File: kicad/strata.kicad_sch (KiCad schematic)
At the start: 107 parts, among them J1 Eurorack Mono Jack, J10 Conn_01x04_Male, J11 Conn_01x04_Male, J12 Conn_01x04_Female, J13 Conn_01x08_Male, J14 Eurorack Mono Jack, J15 Conn_01x08_Female, J16 Eurorack Mono Jack, J17 Eurorack Mono Jack, J18 Eurorack Mono Jack, J19 Eurorack Mono Jack, J2 Eurorack Mono Jack, J20 Eurorack Mono Jack, J24 Eurorack Mono Jack, J25 Eurorack Mono Jack, J26 Eurorack Mono Jack, J27 Eurorack Mono Jack, J28 Eurorack Mono Jack, J29 Eurorack Mono Jack, J3 Eurorack Mono Jack, J30 Eurorack Mono Jack, J31 Eurorack Mono Jack, J32 Conn_01x06_Female, J33 Eurorack Mono Jack, J34 Conn_01x06_Male, J35 Conn_01x08_Female, J36 Conn_01x08_Male, J37 Eurorack Power Small, J38 Conn_02x04_Odd_Even, J39 Conn_01x03_Male, J4 Eurorack Mono Jack, J49 Eurorack Mono Jack, J5 Conn_01x04_Female, J50 Eurorack Mono Jack, J51 Eurorack Mono Jack, J52 Conn_01x04_Female, J53 Conn_01x04_Male, J6 Conn_01x06_Female, J7 Conn_01x04_Male, J8 Conn_01x06_Male, J9 Conn_01x04_Female, U1 TL074, U2 L78L05_TO92

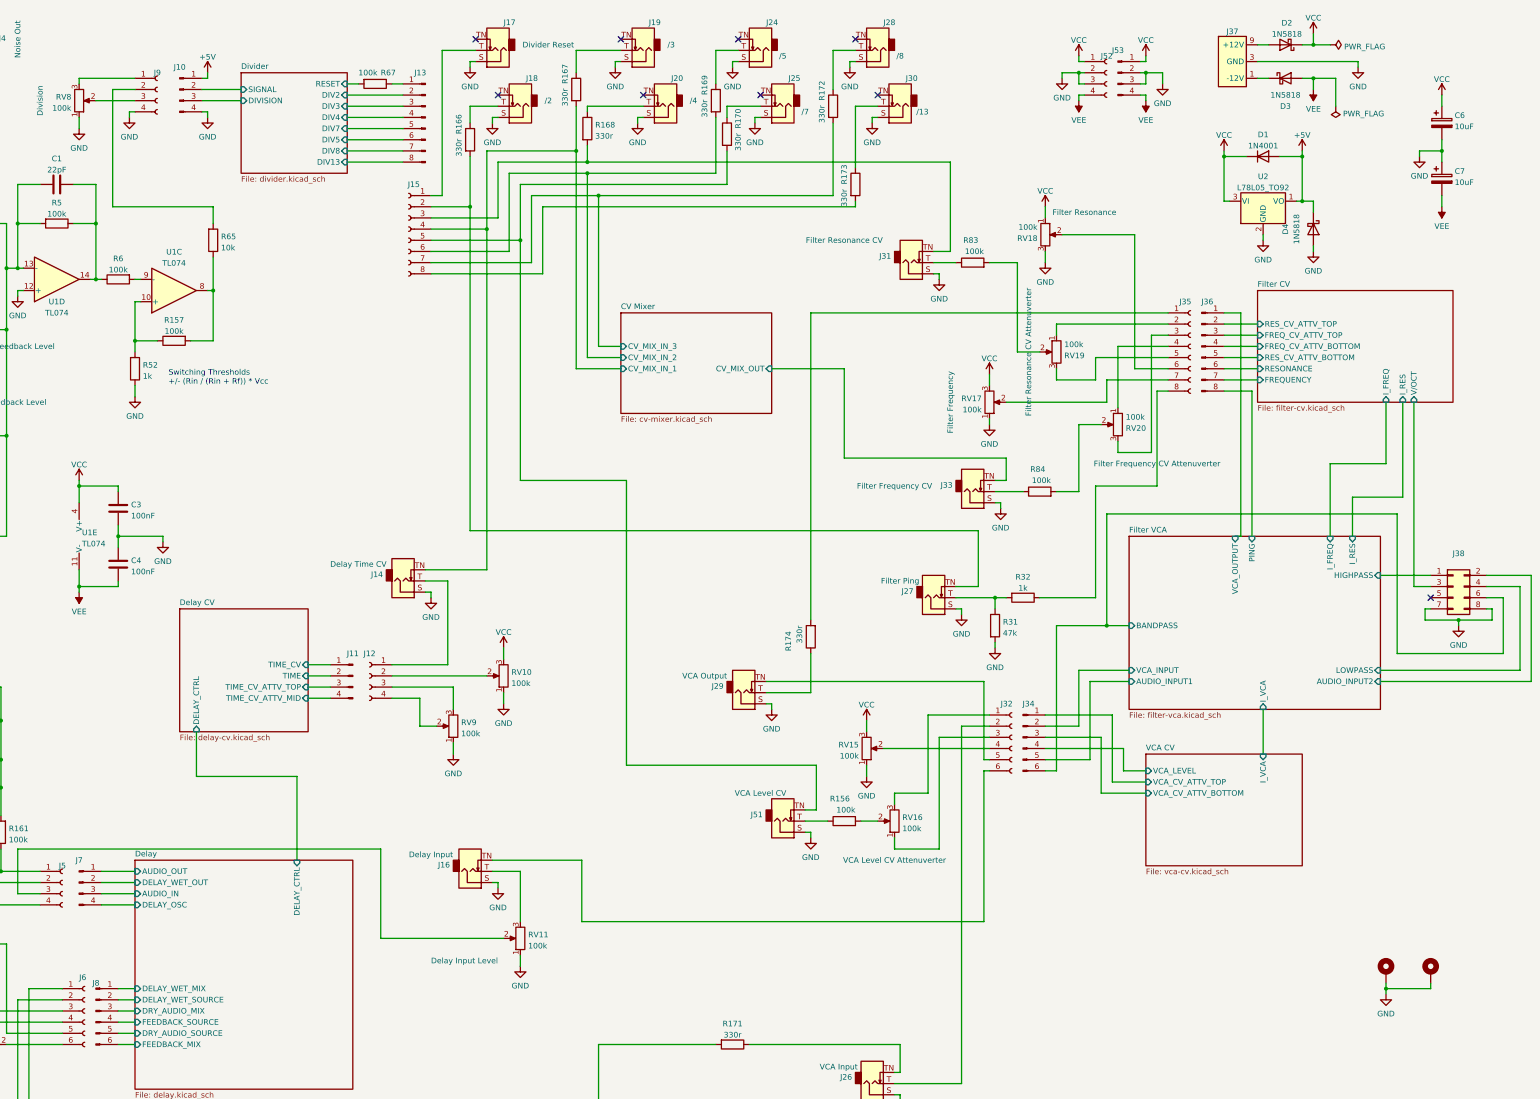
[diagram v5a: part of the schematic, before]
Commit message: Layout seems to be all done, though needs further checking
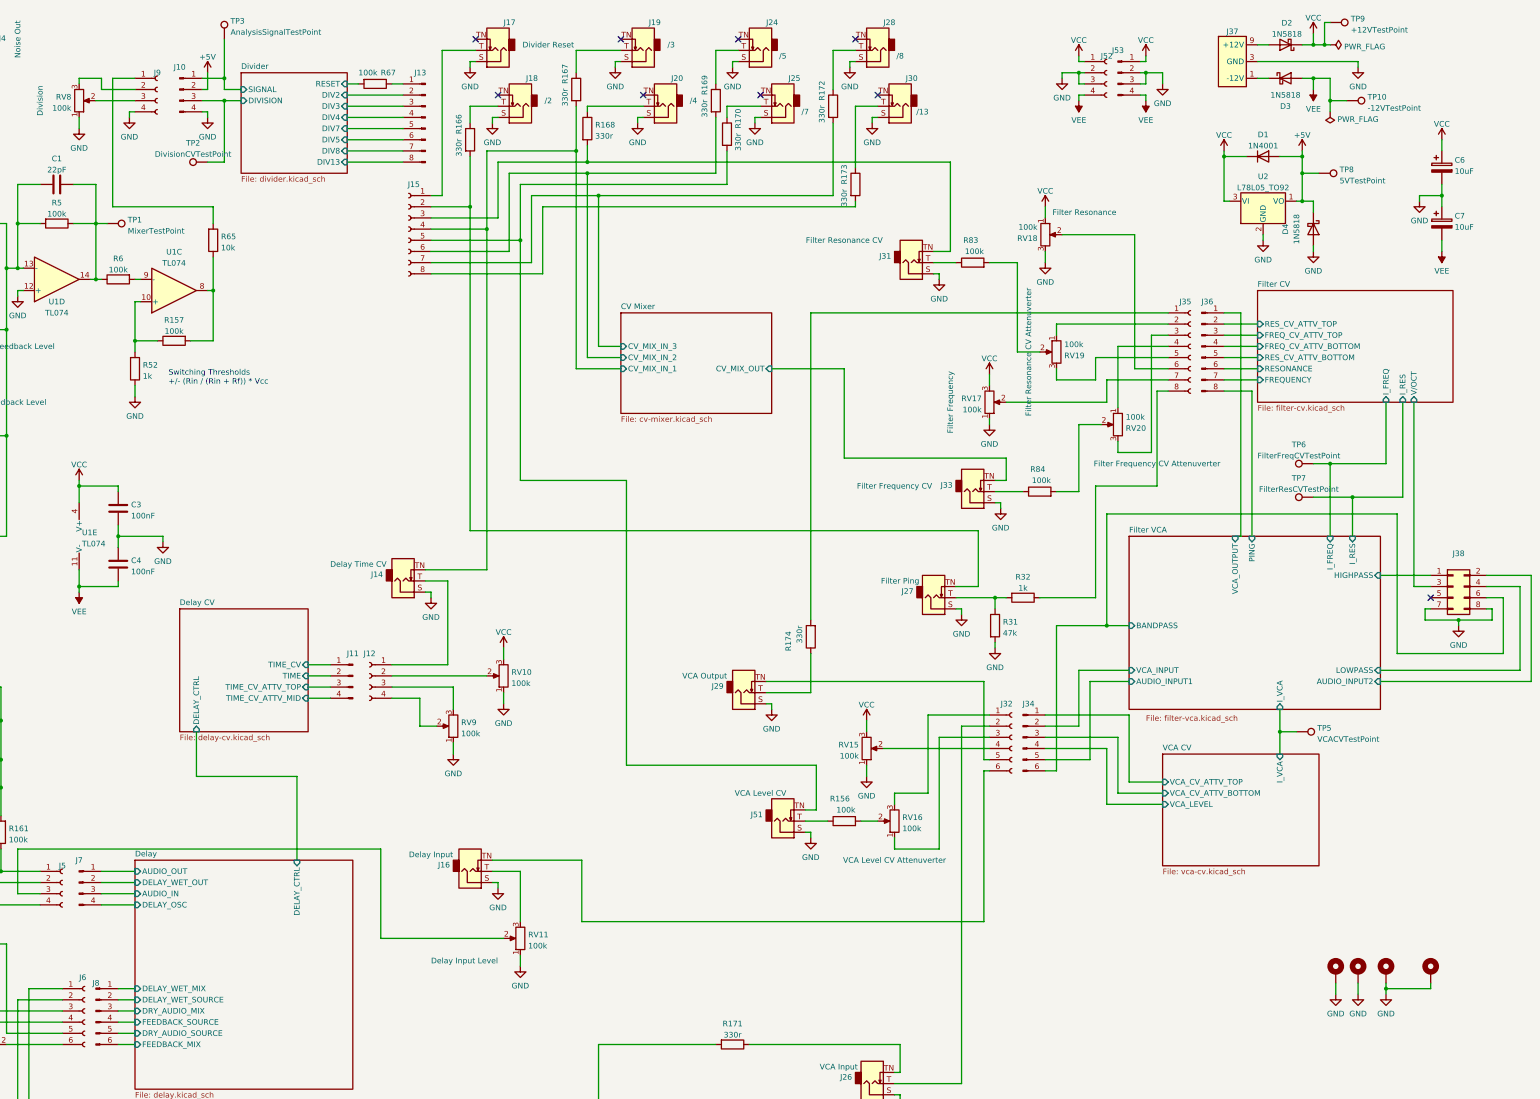
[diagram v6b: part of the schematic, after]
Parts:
- added H2, H4: MountingHole_Pad, rumblesan-standard-parts:MountingHole_3.2mm_M3_DIN965_Pad, symbol Mechanical:MountingHole_Pad
- added TP1: MixerTestPoint, rumblesan-standard-parts:TestPoint_Loop_D2.50mm_Drill1.0mm_LowProfile, symbol Connector:TestPoint
- added TP10: -12VTestPoint, rumblesan-standard-parts:TestPoint_Loop_D2.50mm_Drill1.0mm_LowProfile, symbol Connector:TestPoint
- added TP2: DivisionCVTestPoint, rumblesan-standard-parts:TestPoint_Loop_D2.50mm_Drill1.0mm_LowProfile, symbol Connector:TestPoint
- added TP3: AnalysisSignalTestPoint, rumblesan-standard-parts:TestPoint_Loop_D2.50mm_Drill1.0mm_LowProfile, symbol Connector:TestPoint
- added TP5: VCACVTestPoint, rumblesan-standard-parts:TestPoint_Loop_D2.50mm_Drill1.0mm_LowProfile, symbol Connector:TestPoint
- added TP6: FilterFreqCVTestPoint, rumblesan-standard-parts:TestPoint_Loop_D2.50mm_Drill1.0mm_LowProfile, symbol Connector:TestPoint
- added TP7: FilterResCVTestPoint, rumblesan-standard-parts:TestPoint_Loop_D2.50mm_Drill1.0mm_LowProfile, symbol Connector:TestPoint
- added TP8: 5VTestPoint, rumblesan-standard-parts:TestPoint_Loop_D2.50mm_Drill1.0mm_LowProfile, symbol Connector:TestPoint
- added TP9: +12VTestPoint, rumblesan-standard-parts:TestPoint_Loop_D2.50mm_Drill1.0mm_LowProfile, symbol Connector:TestPoint
- C7: footprint rumblesan-standard-parts:CP_Radial_D6.3.0mm_L11.0mm_P2.00mm_Horizontal -> rumblesan-standard-parts:CP_Radial_D5.0mm_L11.0mm_P2.00mm_Horizontal
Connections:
- net +5V: now also J10.2 (Pin_2), TP8.1; no longer J10.1 (Pin_1)
- net Divider/DIVISION: now also TP2.1
- net Divider/SIGNAL: now also J10.1 (Pin_1), TP3.1; no longer J10.2 (Pin_2)
- net Filter CV/I_FREQ: now also TP6.1
- net Filter CV/I_RES: now also TP7.1
- net Filter VCA/I_VCA: now also TP5.1
- net GND: now also H2.1, H4.1
- net VCC: now also TP9.1
- net VEE: now also TP10.1
- net at R65.2: now also J9.1 (Pin_1); no longer J9.2 (Pin_2)
- net at C1.2, R5.1, R6.1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: now also TP1.1
- net at RV8.3: now also J9.2 (Pin_2); no longer J9.1 (Pin_1)
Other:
- moved on the sheet: C6, C7

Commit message: Updating layout again
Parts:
- removed D1: 1N4001, rumblesan-standard-parts:D_DO-41_SOD81_P10.16mm_Horizontal, symbol Diode:1N4001
- removed R6: 100k, rumblesan-standard-parts:R_Axial_DIN0207_L6.3mm_D2.5mm_P10.16mm_Horizontal, symbol rumblesan-standard-parts:R
- added TP11, TP12, TP16, TP4: GNDTestPoint, rumblesan-standard-parts:TestPoint_Loop_D2.50mm_Drill1.0mm_LowProfile, symbol Connector:TestPoint
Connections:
- net GND: now also TP11.1, TP12.1, TP16.1, TP4.1
- net at C1.2, R5.1, TP1.1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: now also U1.9 (-)

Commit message: Tweaking VCA circuit
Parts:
- added R6: 120k, rumblesan-standard-parts:R_Axial_DIN0207_L6.3mm_D2.5mm_P10.16mm_Horizontal, symbol rumblesan-standard-parts:R
- R156: value 100k -> 330k
- R52: value 1k -> 4k7
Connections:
- net VCC: now also R6.2; no longer RV15.3
- new net: R6.1, RV15.3
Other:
- moved on the sheet: J27, J29, J33, R174, R31, R32, R84, RV17, TP11, TP12, TP4
